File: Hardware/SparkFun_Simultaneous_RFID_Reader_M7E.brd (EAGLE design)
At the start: 35.6 x 61 mm, 72 parts, among them J5 U.FL, U1 UHF_RFID_NANO_MODULE_M7E_HECTO, U2 CH340C

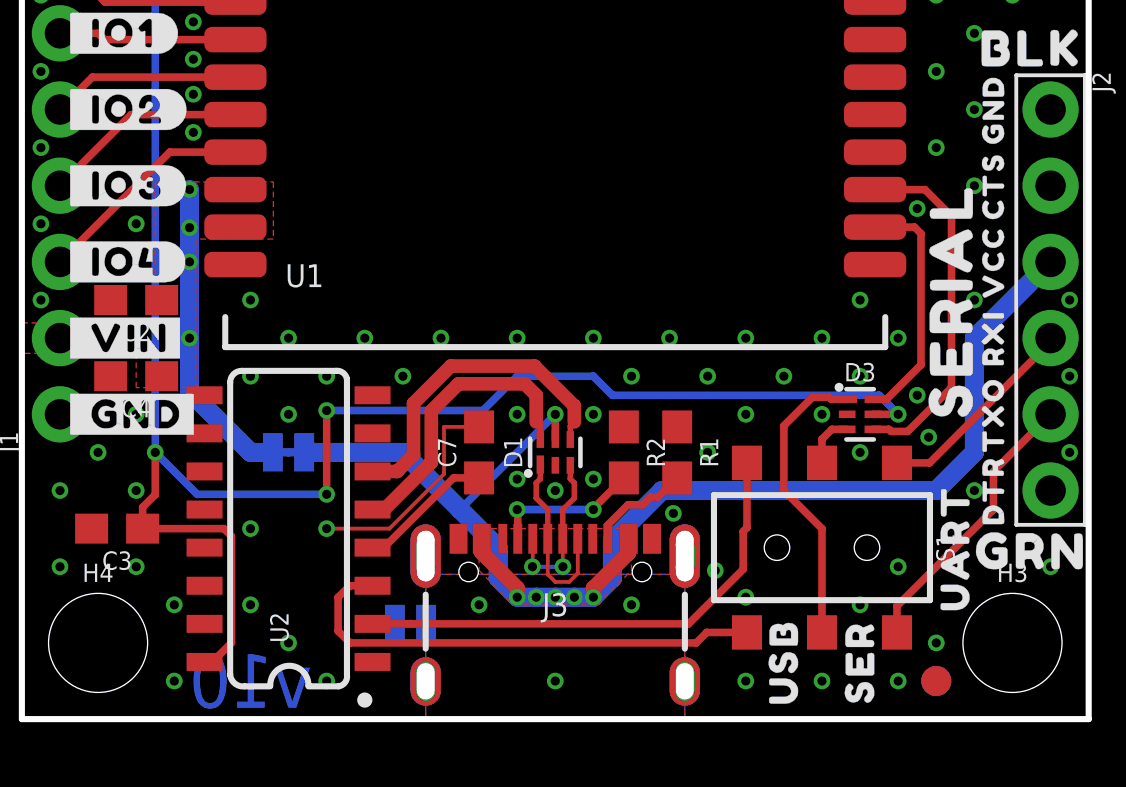
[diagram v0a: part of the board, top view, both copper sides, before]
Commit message: Change VIN selection jumper
Now uses a 3-way jumper to independently select USB, VCC from serial head, or just dedicated VIN pin
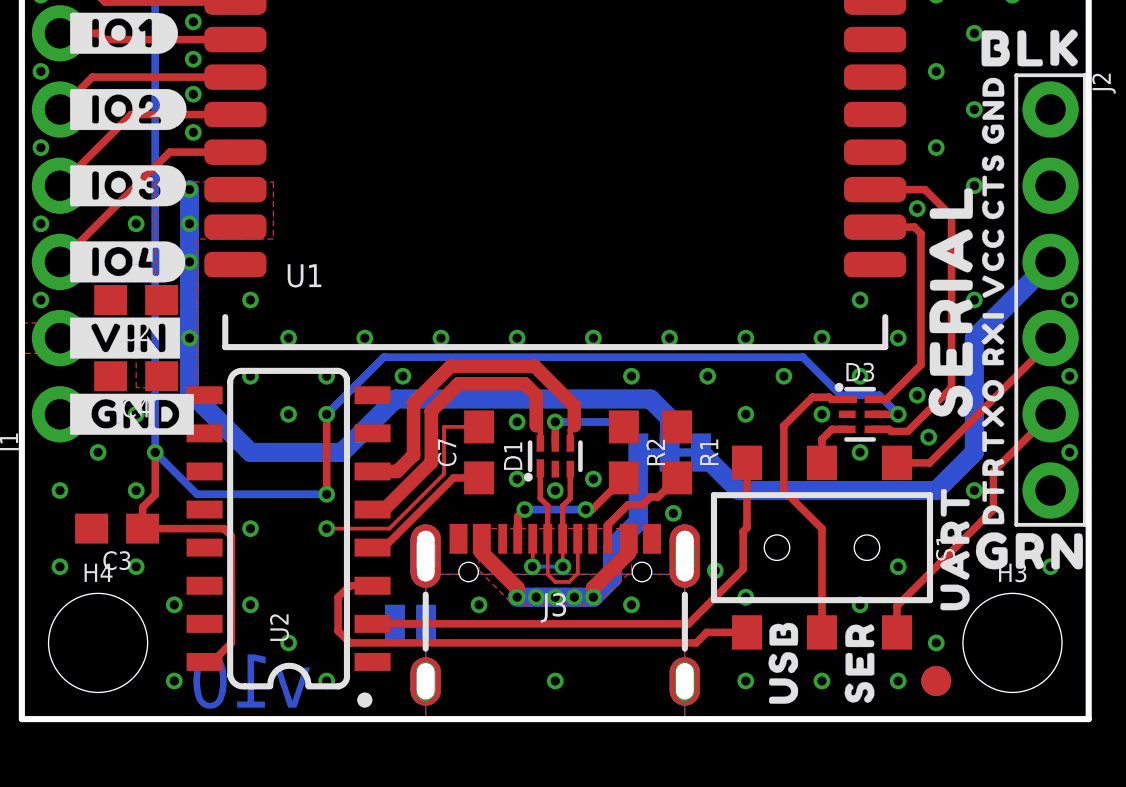
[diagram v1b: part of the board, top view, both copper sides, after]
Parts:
- removed U$51: (no value), output:#VIN#0
- removed VIN: JUMPER-SMT_2_NC_TRACE_SILK, SparkFun-Jumpers:SMT-JUMPER_2_NC_TRACE_SILK
- added U$17: (no value), output:#VIN_SEL#0
- added U$3: (no value), output:#USB#0
- added U$4: (no value), output:#VCC#0
- added VIN_SEL: JUMPER-SMT_3_2-NC_TRACE_SILK, SparkFun-Jumpers:SMT-JUMPER_3_2-NC_TRACE_SILK
- moved U$57 1.27 mm to (17.8, 12.1)
- moved D1 0.13 mm to (17.8, 8.76)
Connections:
- new net VCC: J2.3, VIN_SEL.1
- net VIN: now also VIN_SEL.2; no longer VIN.2
- net V_USB: now also VIN_SEL.3; no longer J2.3, VIN.1
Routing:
- net V_USB: track 45.3 -> 16.9 mm
- net VCC: track 0.00 -> 17.6 mm
- net VIN: track 10.4 -> 25.7 mm
- net GND: vias 215 -> 213

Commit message: Change 3.3V net to VOUT
The M7E internal regulator actually outputs 2.5V when idle
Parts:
- removed U$21: (no value), output:#3V3_#0
- added U$18: (no value), output:#VO#0
- U$9: device output:#_3V3#0 -> output:#VO#1
- flipped U$9 to the bottom
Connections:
- net 3.3V renamed VOUT
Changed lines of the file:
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@@
 <element name="LOGO3" library="SparkFun-Aesthetics" package="SFE_LOGO_NAME_FLAME_.2" value="SFE_LOGO_NAME_FLAME.2_INCH" x="17.78" y="53.34" smashed="yes" rot="MR0"/>
 <element name="U$6" library="output" package="#_GND#0" value="" x="1.27" y="10.16" smashed="yes"/>
-<element name="U$9" library="output" package="#_3V3#0" value="" x="1.27" y="27.94" smashed="yes"/>
 <element name="U$10" library="output" package="#_VIN#0" value="" x="1.27" y="12.7" smashed="yes"/>
 <element name="U$11" library="output" package="#_IO4#0" value="" x="1.27" y="15.24" smashed="yes"/>
@@
 <element name="U$15" library="output" package="#_EN#0" value="" x="1.27" y="25.4" smashed="yes"/>
 <element name="U$27" library="output" package="#GND_#0" value="" x="1.27" y="10.16" smashed="yes" rot="MR0"/>
-<element name="U$21" library="output" package="#3V3_#0" value="" x="1.27" y="27.94" smashed="yes" rot="MR0"/>
 <element name="U$39" library="output" package="#EN_#0" value="" x="1.27" y="25.4" smashed="yes" rot="MR0"/>
 <element name="U$40" library="output" package="#IO1_#0" value="" x="1.27" y="22.86" smashed="yes" rot="MR0"/>
@@
 <element name="U$4" library="output" package="#VCC#0" value="" x="22.987" y="8.89" smashed="yes" rot="MR0"/>
 <element name="U$17" library="output" package="#VIN_SEL#0" value="" x="21.59" y="7.239" smashed="yes" rot="MR0"/>
+<element name="U$18" library="output" package="#VO#0" value="" x="1.27" y="27.94" smashed="yes"/>
+<element name="U$9" library="output" package="#VO#1" value="" x="1.27" y="27.94" smashed="yes" rot="MR0"/>
 </elements>
 <signals>
@@
 <wire x1="20.5486" y1="6.5786" x2="19.685" y2="5.715" width="0.635" layer="16"/>
 </signal>
-<signal name="3.3V">
-<contactref element="U2" pad="16"/>
-<contactref element="U1" pad="10"/>
-<wire x1="7.1175" y1="25.15" x2="4.445" y2="25.15" width="0.254" layer="1"/>
-<wire x1="4.06" y1="25.15" x2="4.445" y2="25.15" width="0.254" layer="1"/>
-<via x="4.445" y="25.15" extent="1-16" drill="0.3048"/>
-<wire x1="4.445" y1="8.89" x2="4.445" y2="25.15" width="0.254" layer="16"/>
-<contactref element="C3" pad="1"/>
-<wire x1="4.445" y1="7.4812" x2="4.025" y2="7.0612" width="0.254" layer="1"/>
-<wire x1="4.025" y1="6.35" x2="4.025" y2="7.0612" width="0.254" layer="1"/>
-<wire x1="4.445" y1="8.89" x2="4.445" y2="7.4812" width="0.254" layer="1"/>
-<via x="4.445" y="8.89" extent="1-16" drill="0.3048"/>
-<wire x1="6.09" y1="1.905" x2="6.35" y2="1.905" width="0.254" layer="1"/>
-<wire x1="6.35" y1="1.905" x2="6.985" y2="2.54" width="0.254" layer="1"/>
-<wire x1="6.985" y1="6.096" x2="6.731" y2="6.35" width="0.254" layer="1"/>
-<wire x1="6.731" y1="6.35" x2="4.025" y2="6.35" width="0.254" layer="1"/>
-<wire x1="6.985" y1="2.54" x2="6.985" y2="6.096" width="0.254" layer="1"/>
-<contactref element="D3" pad="5"/>
-<wire x1="4.445" y1="8.89" x2="5.842" y2="7.493" width="0.254" layer="16"/>
-<wire x1="5.842" y1="7.493" x2="10.16" y2="7.493" width="0.254" layer="16"/>
-<via x="10.16" y="7.493" extent="1-16" drill="0.3048"/>
-<wire x1="10.16" y1="7.493" x2="10.16" y2="10.16" width="0.254" layer="1"/>
-<via x="10.16" y="10.16" extent="1-16" drill="0.3048"/>
-<wire x1="28.575" y1="10.795" x2="27.305" y2="10.795" width="0.254" layer="16"/>
-<wire x1="26.035" y1="12.065" x2="27.305" y2="10.795" width="0.254" layer="16"/>
-<wire x1="10.16" y1="10.16" x2="12.065" y2="12.065" width="0.254" layer="16"/>
-<wire x1="12.065" y1="12.065" x2="26.035" y2="12.065" width="0.254" layer="16"/>
-<contactref element="J1" pad="8"/>
-<wire x1="1.27" y1="27.94" x2="4.06" y2="25.15" width="0.254" layer="1"/>
-<contactref element="R3" pad="2"/>
-<wire x1="28.37" y1="10.16" x2="29.21" y2="10.16" width="0.254" layer="1"/>
-<via x="29.21" y="10.16" extent="1-16" drill="0.3048"/>
-<wire x1="29.21" y1="10.16" x2="28.575" y2="10.795" width="0.254" layer="16"/>
-<wire x1="1.27" y1="27.94" x2="1.69" y2="28.36" width="0.254" layer="1"/>
-<wire x1="1.69" y1="28.36" x2="1.69" y2="29.845" width="0.254" layer="1"/>
-</signal>
 <signal name="N$3">
 <contactref element="R1" pad="2"/>
@@
 <wire x1="30.48" y1="7.62" x2="23.9014" y2="7.62" width="0.635" layer="16"/>
 </signal>
+<signal name="VOUT">
+<contactref element="U1" pad="10"/>
+<contactref element="J1" pad="8"/>
+<via x="4.445" y="25.146" extent="1-16" drill="0.3048"/>
+<wire x1="4.445" y1="25.146" x2="4.064" y2="25.146" width="0.254" layer="1"/>
+<wire x1="4.064" y1="25.146" x2="1.27" y2="27.94" width="0.254" layer="1"/>
+<wire x1="7.1175" y1="25.15" x2="7.1135" y2="25.146" width="0.254" layer="1"/>
+<wire x1="7.1135" y1="25.146" x2="4.445" y2="25.146" width="0.254" layer="1"/>
+<wire x1="4.445" y1="25.146" x2="4.445" y2="8.89" width="0.254" layer="16"/>
+<contactref element="U2" pad="16"/>
+<contactref element="C3" pad="1"/>
+<wire x1="6.09" y1="1.905" x2="6.35" y2="1.905" width="0.254" layer="1"/>
+<wire x1="6.35" y1="1.905" x2="6.985" y2="2.54" width="0.254" layer="1"/>
+<wire x1="6.985" y1="6.096" x2="6.731" y2="6.35" width="0.254" layer="1"/>
+<wire x1="6.731" y1="6.35" x2="4.064" y2="6.35" width="0.254" layer="1"/>
+<wire x1="4.064" y1="6.35" x2="4.025" y2="6.35" width="0.254" layer="1"/>
+<wire x1="6.985" y1="2.54" x2="6.985" y2="6.096" width="0.254" layer="1"/>
+<via x="4.445" y="8.89" extent="1-16" drill="0.3048"/>
+<wire x1="4.445" y1="7.493" x2="4.064" y2="7.112" width="0.254" layer="1"/>
+<wire x1="4.064" y1="7.112" x2="4.064" y2="6.35" width="0.254" layer="1"/>
+<wire x1="4.445" y1="8.89" x2="4.445" y2="7.493" width="0.254" layer="1"/>
+<wire x1="4.445" y1="8.89" x2="5.842" y2="7.493" width="0.254" layer="16"/>
+<wire x1="10.16" y1="7.493" x2="5.842" y2="7.493" width="0.254" layer="16"/>
+<contactref element="D3" pad="5"/>
+<via x="10.16" y="7.493" extent="1-16" drill="0.3048"/>
+<wire x1="10.16" y1="7.493" x2="10.16" y2="10.16" width="0.254" layer="1"/>
+<via x="10.16" y="10.16" extent="1-16" drill="0.3048"/>
+<wire x1="28.575" y1="10.795" x2="27.305" y2="10.795" width="0.254" layer="16"/>
+<wire x1="26.035" y1="12.065" x2="27.305" y2="10.795" width="0.254" layer="16"/>
+<wire x1="10.16" y1="10.16" x2="12.065" y2="12.065" width="0.254" layer="16"/>
+<wire x1="12.065" y1="12.065" x2="26.035" y2="12.065" width="0.254" layer="16"/>
+<wire x1="28.37" y1="10.16" x2="29.21" y2="10.16" width="0.254" layer="1"/>
+<via x="29.21" y="10.16" extent="1-16" drill="0.3048"/>
+<wire x1="29.21" y1="10.16" x2="28.575" y2="10.795" width="0.254" layer="16"/>
+<contactref element="R3" pad="2"/>
+<wire x1="1.69" y1="28.36" x2="1.69" y2="29.845" width="0.254" layer="1"/>
+<wire x1="1.27" y1="27.94" x2="1.69" y2="28.36" width="0.254" layer="1"/>
+</signal>
 </signals>

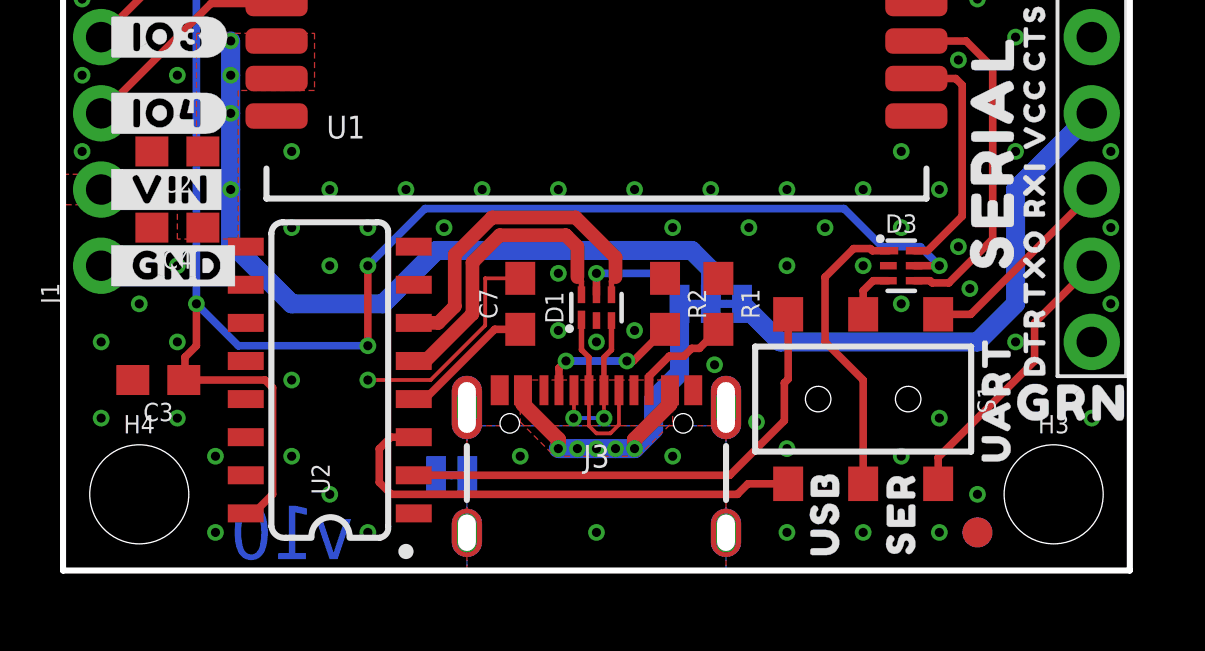
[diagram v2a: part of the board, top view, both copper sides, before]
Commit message: Fix CH340 power
Can't be powered by VOUT, because the module outputs 2.5V while idle, which is too low for the CH340
Now powered by VUSB.  The only problem here is that the output voltage is based on VCC, so a voltage divider is used to make the output voltage ~3.3V
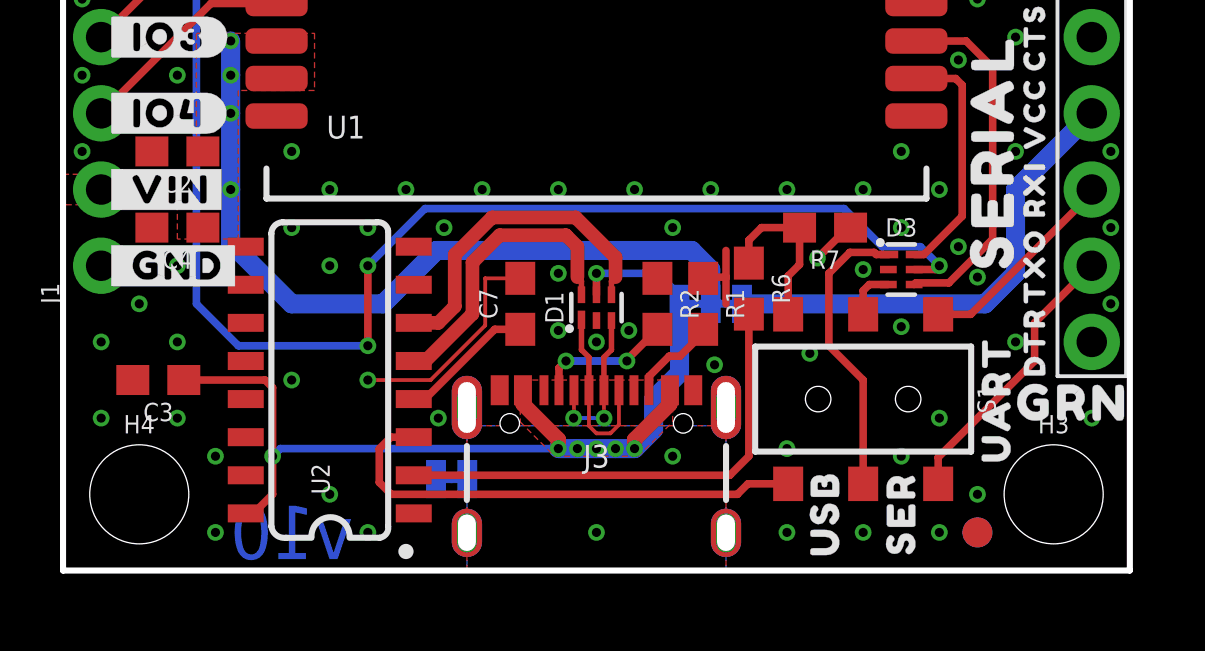
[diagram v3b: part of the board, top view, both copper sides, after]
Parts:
- added R6: 5.1k, SparkFun-Resistors:0603
- added R7: 10k, SparkFun-Resistors:0603
- moved R1 0.51 mm to (21.3, 8.89)
- moved R2 0.25 mm to (19.8, 8.89)
- moved D3 0.13 mm to (27.9, 10.0)
- moved SHLD 0.13 mm to (13.0, 3.05)
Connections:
- new net N$14: R6.2, U2.2
- net GND: now also R7.1
- net RX_USB: now also R6.1, R7.2; no longer U2.2
- net VOUT: no longer C3.1, U2.16
- net V_USB: now also C3.1, U2.16
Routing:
- net V_USB: track 16.9 -> 34.3 mm, vias 6 -> 7
- net N$14: track 0.00 -> 16.2 mm
- net RX_USB: track 16.7 -> 5.67 mm
- net VOUT: track 66.2 -> 55.8 mm, vias 5 -> 4
- net GND: track 10.4 -> 14.5 mm, vias 213 -> 211
- net VCC: track 17.6 -> 15.9 mm
